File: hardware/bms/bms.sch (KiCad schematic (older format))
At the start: 8 parts

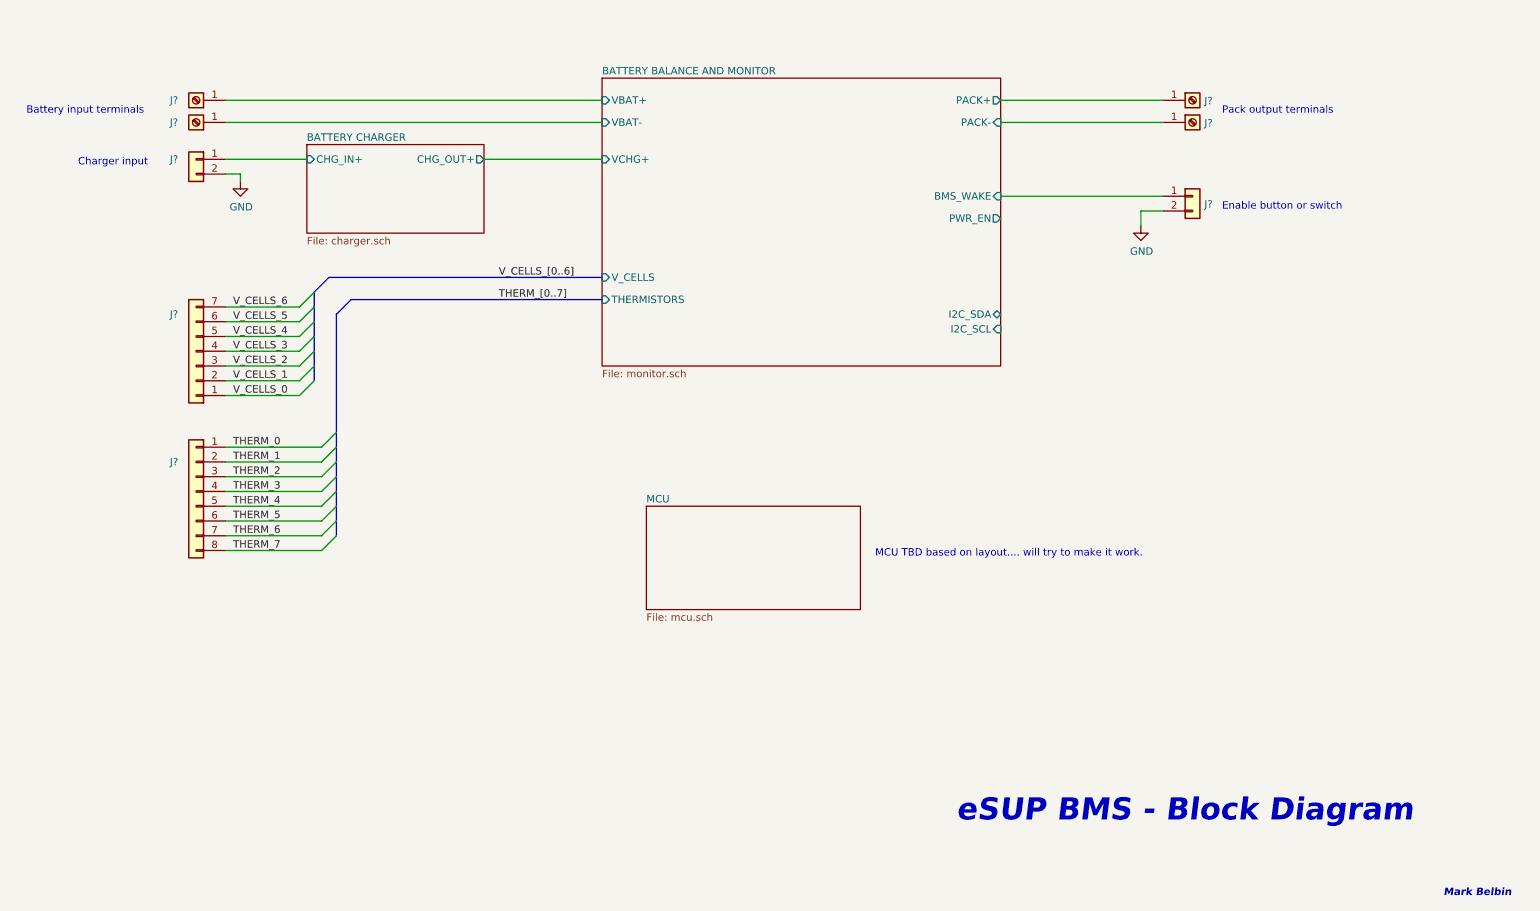
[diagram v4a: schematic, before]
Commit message: Selected connectors for cell taps, in/out power, charger, and enable switch.
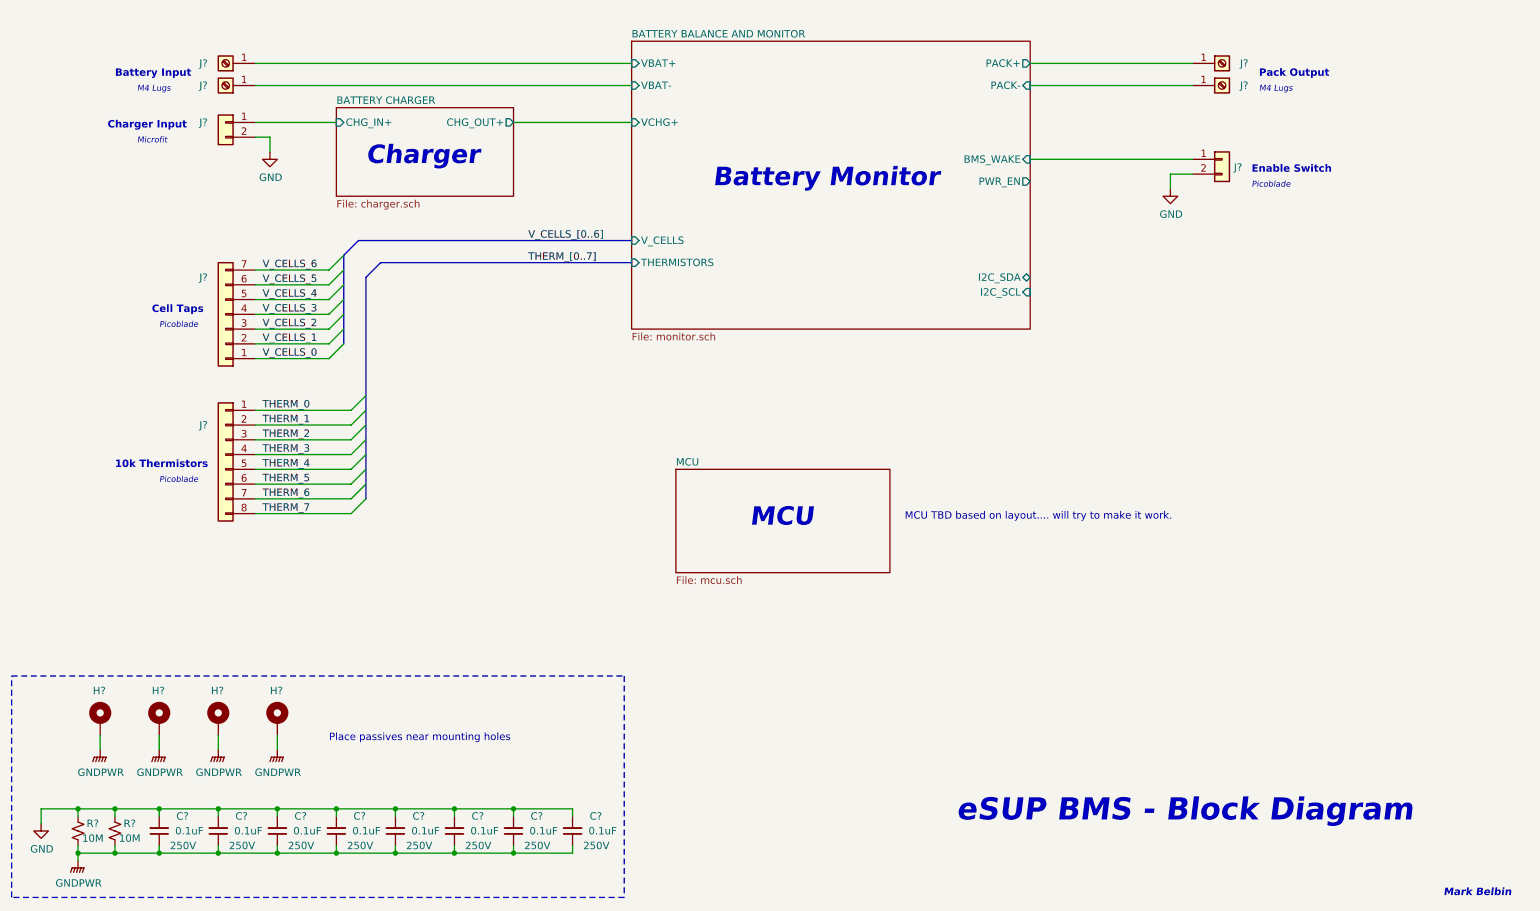
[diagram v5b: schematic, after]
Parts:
- removed J? (x3): Screw_Terminal_01x01, symbol Connector:Screw_Terminal_01x01
- removed J?: Conn_01x02, symbol Connector_Generic:Conn_01x02
- added C? (x8): 0.1uF, Capacitor_SMD:C_0805_2012Metric, symbol Device:C_Small
- added H? (x4): MountingHole_Pad, MountingHole:MountingHole_3.2mm_M3_Pad_Via, symbol Mechanical:MountingHole_Pad
- added J?: Conn_01x02, symbol Connector_Generic:Conn_01x02
- added J? (x3): Screw_Terminal_01x01, symbol Connector:Screw_Terminal_01x01
- added R? (x2): 10M, Resistor_SMD:R_0603_1608Metric, symbol Device:R_Small_US
- J?: footprint (none) -> Connector_Molex:Molex_PicoBlade_53261-0271_1x02-1MP_P1.25mm_Horizontal; MFG (none) -> Molex; MFG PN (none) -> 0532610271
- J?: MFG (none) -> Würth Elektronik; MFG PN (none) -> 7466114
- J?: footprint (none) -> Connector_Molex:Molex_PicoBlade_53261-0871_1x08-1MP_P1.25mm_Horizontal; MFG (none) -> Molex; MFG PN (none) -> 0532610871
- J?: footprint (none) -> Connector_Molex:Molex_PicoBlade_53261-0771_1x07-1MP_P1.25mm_Horizontal; MFG (none) -> Molex; MFG PN (none) -> 0532610771
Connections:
- net BATTERY BALANCE AND MONITOR/PACK+: now also J?.1 (Pin_1)
- net BATTERY BALANCE AND MONITOR/PACK-: now also J?.1 (Pin_1)
- net BATTERY BALANCE AND MONITOR/VBAT-: now also J?.1 (Pin_1)
- net BATTERY CHARGER/CHG_IN+: now also J?.1 (Pin_1)
- net GND: now also C?.2, C?.2, C?.2, C?.2, C?.2, C?.2, C?.2, C?.2, J?.2 (Pin_2), R?.1, R?.1
- new net GNDPWR: C?.1, C?.1, C?.1, C?.1, C?.1, C?.1, C?.1, C?.1, H?.1, H?.1, H?.1, H?.1, R?.2, R?.2
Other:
- note added: "10k Thermistors"
- note added: "Battery Input"
- note added: "Battery Monitor"
- note added: "Cell Taps"
- note added: "Charger"
- note added: "Charger Input"
- note added: "Enable Switch"
- note added: "M4 Lugs"
- note added: "MCU"
- note added: "Microfit"
- note added: "Pack Output"
- note added: "Picoblade"
- note added: "Place passives near mounting holes"
- note removed: "Battery input terminals"
- note removed: "Charger input"
- note removed: "Enable button or switch"
- note removed: "Pack output terminals"
- moved on the sheet: J?

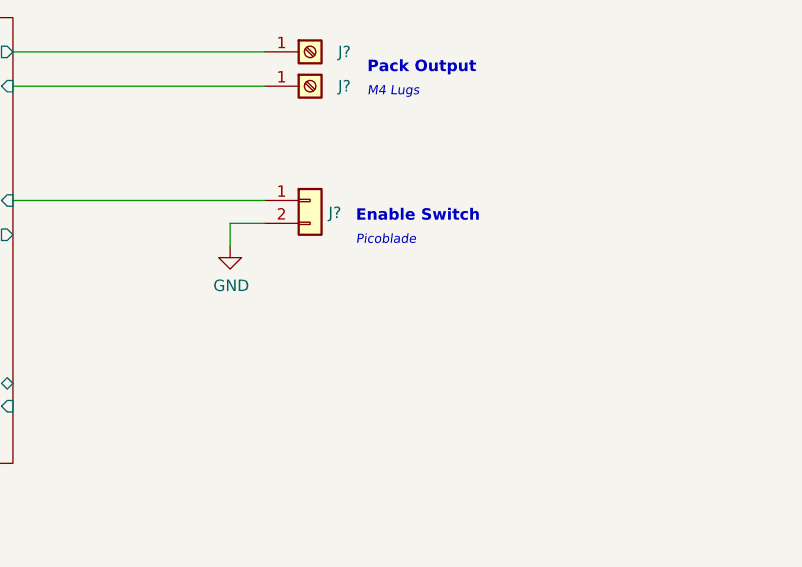
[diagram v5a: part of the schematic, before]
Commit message: Created footprints for microfit and wurth screw terminals
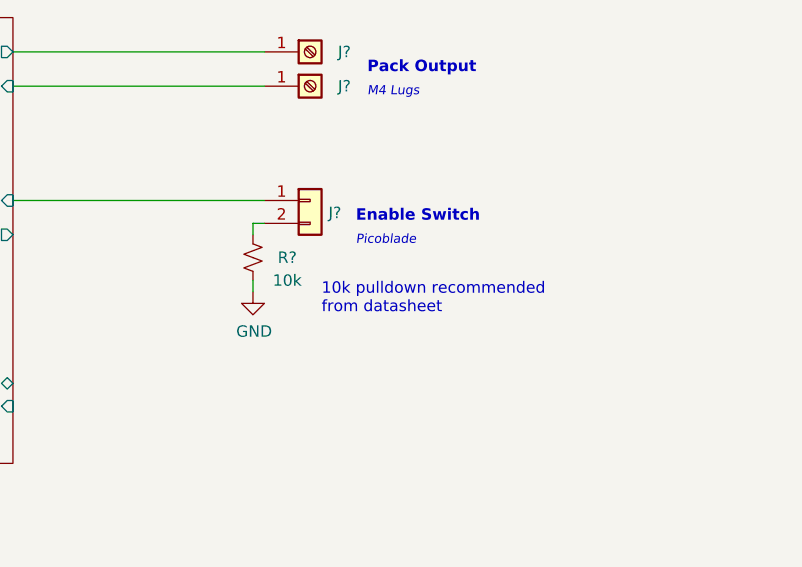
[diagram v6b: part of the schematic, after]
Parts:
- removed J? (x3): Screw_Terminal_01x01, symbol Connector:Screw_Terminal_01x01
- added J? (x3): Screw_Terminal_01x01, bms:Wurth_746600430R, symbol Connector:Screw_Terminal_01x01
- added R?: 10k, Resistor_SMD:R_0603_1608Metric, symbol Device:R_Small_US
- J?: footprint (none) -> bms:MOLEX_436500214
- J?: footprint (none) -> bms:Wurth_746600430R; MFG PN 7466114 -> 746600430R
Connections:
- net BATTERY BALANCE AND MONITOR/PACK+: now also J?.1 (Pin_1)
- net BATTERY BALANCE AND MONITOR/PACK-: now also J?.1 (Pin_1)
- net BATTERY BALANCE AND MONITOR/VBAT+: now also J?.1 (Pin_1)
- net GND: now also R?.2; no longer J?.2 (Pin_2)
- new net: J?.2 (Pin_2), R?.1
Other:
- note added: "10k pulldown recommended\nfrom datasheet"
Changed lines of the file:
@@
 	8800 2500 7700 2500
 Wire Wire Line
-	8800 2600 8650 2600
-Wire Wire Line
-	8650 2600 8650 2700
+	8800 2600 8750 2600
 $Comp
 L power:GND #PWR?
 U 1 1 6657629A
-P 8650 2700
-F 0 "#PWR?" H 8650 2450 50  0001 C CNN
-F 1 "GND" H 8655 2527 50  0000 C CNN
-F 2 "" H 8650 2700 50  0001 C CNN
-F 3 "" H 8650 2700 50  0001 C CNN
-	1    8650 2700
-	1    0    0    -1
-$EndComp
-$Comp
-L Connector:Screw_Terminal_01x01 J?
-U 1 1 66576976
-P 2250 1850
-F 0 "J?" H 2400 1850 50  0000 C CNN
-F 1 "Screw_Terminal_01x01" H 2330 1801 50  0001 L CNN
-F 2 "" H 2250 1850 50  0001 C CNN
-F 3 "~" H 2250 1850 50  0001 C CNN
-F 4 "Würth Elektronik" H 2250 1850 50  0001 C CNN "MFG"
-F 5 "7466114" H 2250 1850 50  0001 C CNN "MFG PN"
-	1    2250 1850
-	-1   0    0    1
+P 8750 2900
+F 0 "#PWR?" H 8750 2650 50  0001 C CNN
+F 1 "GND" H 8755 2727 50  0000 C CNN
+F 2 "" H 8750 2900 50  0001 C CNN
+F 3 "" H 8750 2900 50  0001 C CNN
+	1    8750 2900
+	1    0    0    -1
 $EndComp
 Wire Wire Line
@@
 F 0 "J?" H 2400 2250 50  0000 C CNN
 F 1 "Conn_01x02" H 2330 2151 50  0001 L CNN
-F 2 "" H 2250 2250 50  0001 C CNN
+F 2 "bms:MOLEX_436500214" H 2250 2250 50  0001 C CNN
 F 3 "~" H 2250 2250 50  0001 C CNN
 F 4 "Molex" H 2250 2250 50  0001 C CNN "MFG"
@@
 F 0 "J?" H 2400 2000 50  0000 C CNN
 F 1 "Screw_Terminal_01x01" H 2330 1951 50  0001 L CNN
-F 2 "" H 2250 2000 50  0001 C CNN
+F 2 "bms:Wurth_746600430R" H 2250 2000 50  0001 C CNN
 F 3 "~" H 2250 2000 50  0001 C CNN
 F 4 "Würth Elektronik" H 2250 2000 50  0001 C CNN "MFG"
-F 5 "7466114" H 2250 2000 50  0001 C CNN "MFG PN"
+F 5 "746600430R" H 2250 2000 50  0001 C CNN "MFG PN"
 	1    2250 2000
 	-1   0    0    1
-$EndComp
-$Comp
-L Connector:Screw_Terminal_01x01 J?
-U 1 1 6673152E
-P 9000 1850
-F 0 "J?" H 9150 1850 50  0000 C CNN
-F 1 "Screw_Terminal_01x01" H 9080 1801 50  0001 L CNN
-F 2 "" H 9000 1850 50  0001 C CNN
-F 3 "~" H 9000 1850 50  0001 C CNN
-F 4 "Würth Elektronik" H 9000 1850 50  0001 C CNN "MFG"
-F 5 "7466114" H 9000 1850 50  0001 C CNN "MFG PN"
-	1    9000 1850
-	1    0    0    -1
-$EndComp
-$Comp
-L Connector:Screw_Terminal_01x01 J?
-U 1 1 66733503
-P 9000 2000
-F 0 "J?" H 9150 2000 50  0000 C CNN
-F 1 "Screw_Terminal_01x01" H 9080 1951 50  0001 L CNN
-F 2 "" H 9000 2000 50  0001 C CNN
-F 3 "~" H 9000 2000 50  0001 C CNN
-F 4 "Würth Elektronik" H 9000 2000 50  0001 C CNN "MFG"
-F 5 "7466114" H 9000 2000 50  0001 C CNN "MFG PN"
-	1    9000 2000
-	1    0    0    -1
 $EndComp
 $Comp
@@
 Text Notes 5800 5000 0    125  Italic 25
 MCU
+$Comp
+L Device:R_Small_US R?
+U 1 1 66AA21DD
+P 8750 2750
+AR Path="/6523A805/66AA21DD" Ref="R?"  Part="1"
+AR Path="/66AA21DD" Ref="R?"  Part="1"
+F 0 "R?" H 8900 2750 50  0000 C CNN
+F 1 "10k" H 8900 2650 50  0000 C CNN
+F 2 "Resistor_SMD:R_0603_1608Metric" H 8750 2750 50  0001 C CNN
+F 3 "~" H 8750 2750 50  0001 C CNN
+F 4 "Panasonic Electronic Components" V 8750 2750 50  0001 C CNN "MFG"
+F 5 "ERJ-3GEYJ103V" V 8750 2750 50  0001 C CNN "MFG PN"
+	1    8750 2750
+	1    0    0    -1
+$EndComp
+Wire Wire Line
+	8750 2650 8750 2600
+Wire Wire Line
+	8750 2850 8750 2900
 Wire Bus Line
 	3050 3150 3050 3750
 Wire Bus Line
 	3200 3300 3200 4800
+Text Notes 9050 3000 0    50   ~ 0
+10k pulldown recommended\nfrom datasheet
+$Comp
+L Connector:Screw_Terminal_01x01 J?
+U 1 1 66B13502
+P 2250 1850
+F 0 "J?" H 2400 1850 50  0000 C CNN
+F 1 "Screw_Terminal_01x01" H 2330 1801 50  0001 L CNN
+F 2 "bms:Wurth_746600430R" H 2250 1850 50  0001 C CNN
+F 3 "~" H 2250 1850 50  0001 C CNN
+F 4 "Würth Elektronik" H 2250 1850 50  0001 C CNN "MFG"
+F 5 "746600430R" H 2250 1850 50  0001 C CNN "MFG PN"
+	1    2250 1850
+	-1   0    0    1
+$EndComp
+$Comp
+L Connector:Screw_Terminal_01x01 J?
+U 1 1 66B13F97
+P 9000 1850
+F 0 "J?" H 9150 1850 50  0000 C CNN
+F 1 "Screw_Terminal_01x01" H 9080 1801 50  0001 L CNN
+F 2 "bms:Wurth_746600430R" H 9000 1850 50  0001 C CNN
+F 3 "~" H 9000 1850 50  0001 C CNN
+F 4 "Würth Elektronik" H 9000 1850 50  0001 C CNN "MFG"
+F 5 "746600430R" H 9000 1850 50  0001 C CNN "MFG PN"
+	1    9000 1850
+	1    0    0    -1
+$EndComp
+$Comp
+L Connector:Screw_Terminal_01x01 J?
+U 1 1 66B15AA2
+P 9000 2000
+F 0 "J?" H 9150 2000 50  0000 C CNN
+F 1 "Screw_Terminal_01x01" H 9080 1951 50  0001 L CNN
+F 2 "bms:Wurth_746600430R" H 9000 2000 50  0001 C CNN
+F 3 "~" H 9000 2000 50  0001 C CNN
+F 4 "Würth Elektronik" H 9000 2000 50  0001 C CNN "MFG"
+F 5 "746600430R" H 9000 2000 50  0001 C CNN "MFG PN"
+	1    9000 2000
+	1    0    0    -1
+$EndComp
 $EndSCHEMATC
